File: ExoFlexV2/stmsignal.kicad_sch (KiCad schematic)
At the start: 4 parts, among them J4 CN8, J5 CN9, J6 CN7, J7 CN10

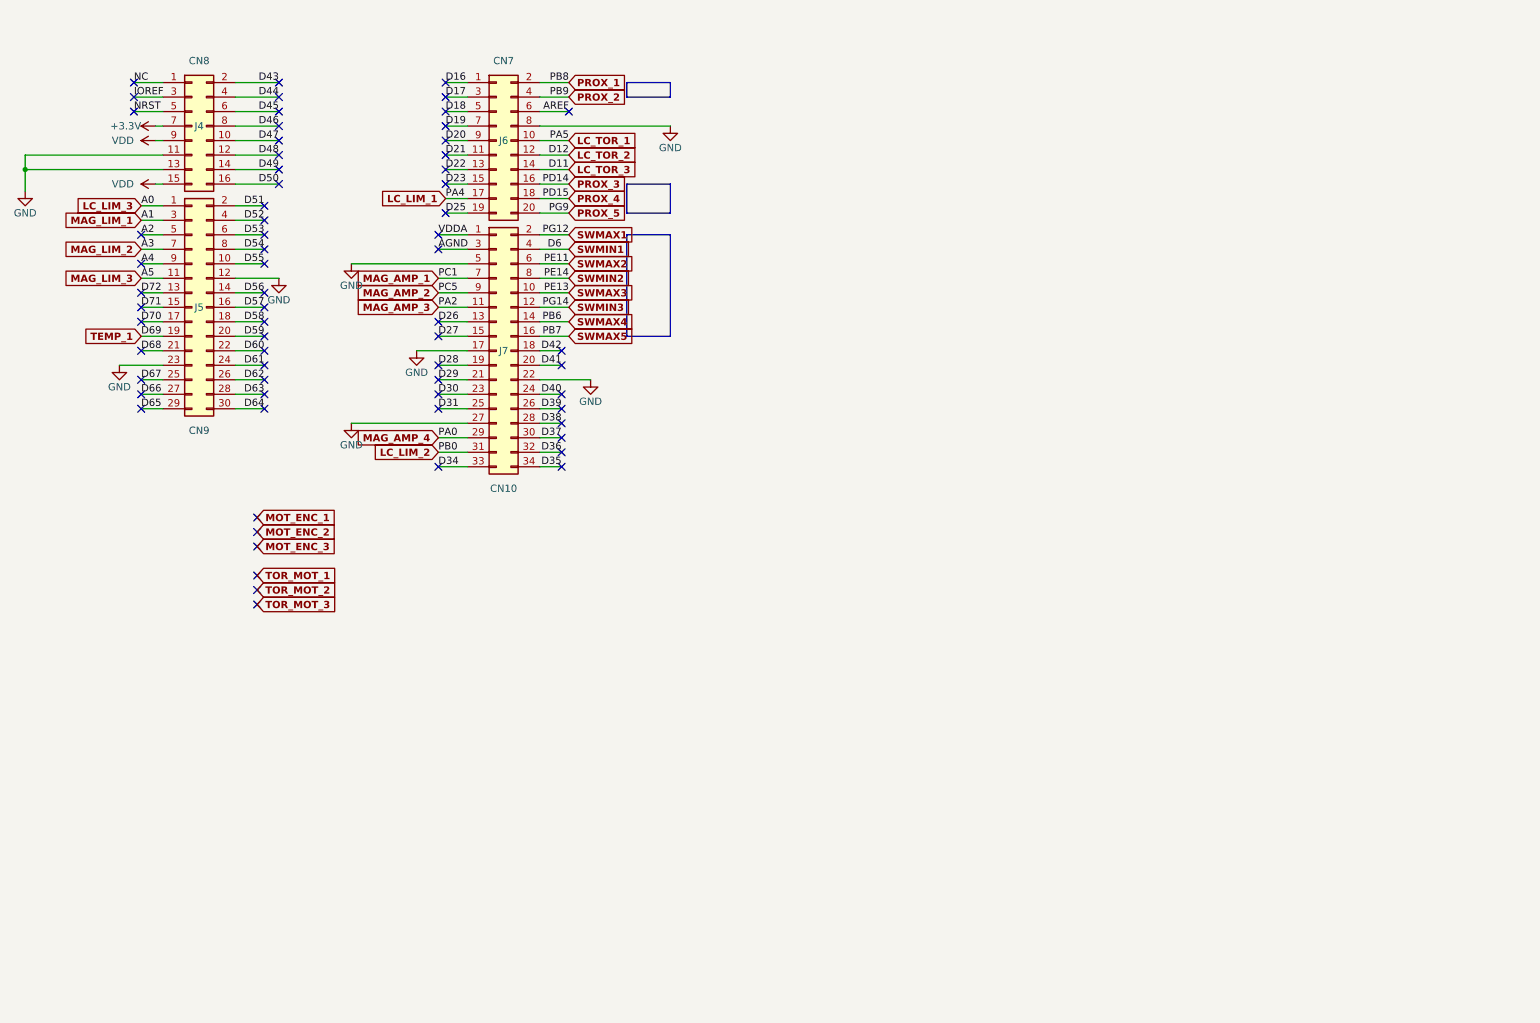
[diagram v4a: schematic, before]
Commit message: Mise à jour mi-stage
- Torque et Amplitude testé et vérifié
- Capteur de présence et de proximité testé
- Système de détection de coupure de fils
- Polyvalence pour plusieurs capteurs
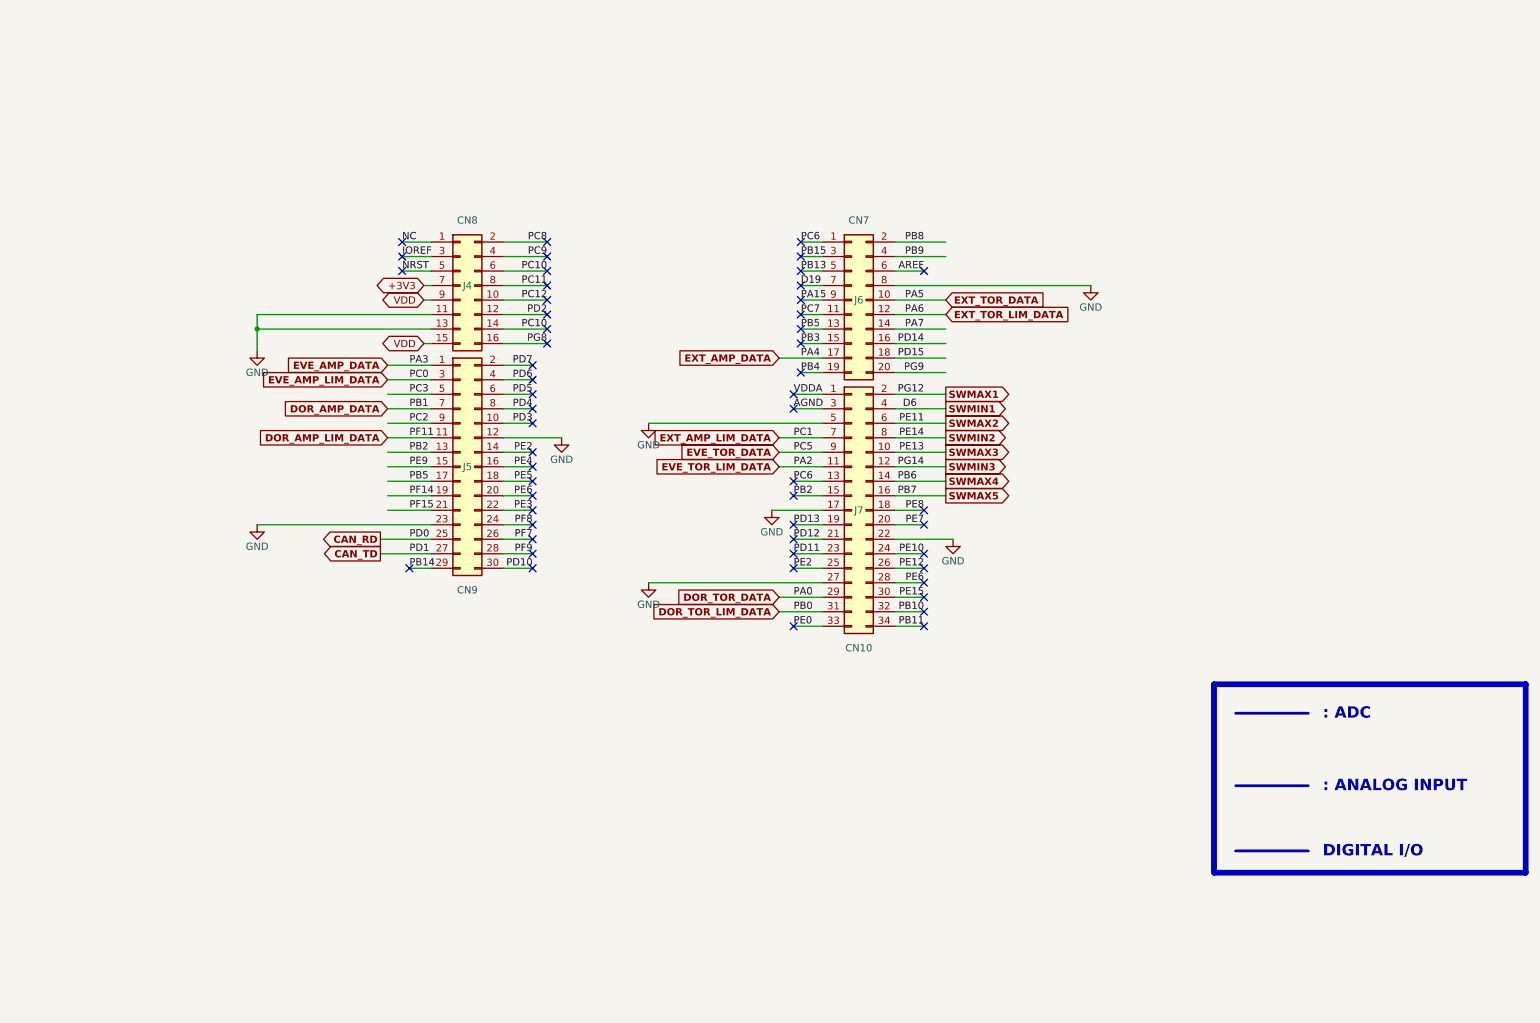
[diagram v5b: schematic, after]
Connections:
- net D26 is gone; now on net PC6: J7.13 (Pin_13)
- net D49 is gone; now on net PC10: J4.14 (Pin_14)
- net D56 is gone; now on net PE2: J5.14 (Pin_14)
- net D59 is gone; now on net PE6: J5.20 (Pin_20)
- net D70 is gone; now on net PB5: J5.17 (Pin_17)
- net D72 is gone; now on net PB2: J5.13 (Pin_13)
- net A2 renamed PC3
- net A4 renamed PC2
- net D16 renamed PC6
- net D17 renamed PB15
- net D18 renamed PB13
- net D20 renamed PA15
- net D21 renamed PC7
- net D22 renamed PB5
- net D23 renamed PB3
- net D25 renamed PB4
- net D27 renamed PB2
- net D28 renamed PD13
- net D29 renamed PD12
- net D30 renamed PD11
- net D31 renamed PE2
- net D34 renamed PE0
- net D35 renamed PB11
- net D36 renamed PB10
- net D37 renamed PE15
- net D38 renamed PE6
- net D39 renamed PE12
- net D40 renamed PE10
- net D41 renamed PE7
- net D42 renamed PE8
- net D43 renamed PC8
- net D44 renamed PC9
- net D45 renamed PC10
- net D46 renamed PC11
- net D47 renamed PC12
- net D48 renamed PD2
- net D50 renamed PG8
- net D51 renamed PD7
- net D52 renamed PD6
- net D53 renamed PD5
- net D54 renamed PD4
- net D55 renamed PD3
- net D57 renamed PE4
- net D58 renamed PE5
- net D60 renamed PE3
- net D61 renamed PF8
- net D62 renamed PF7
- net D63 renamed PF9
- net D64 renamed PD10
- net D65 renamed PB14
- net D66 renamed CAN_TD
- net D67 renamed CAN_RD
- net D68 renamed PF15
- net D71 renamed PE9
- net LC_LIM_1 renamed EXT_AMP_DATA
- net LC_LIM_2 renamed DOR_TOR_LIM_DATA
- net LC_LIM_3 renamed EVE_AMP_DATA
- net LC_TOR_1 renamed EXT_TOR_DATA
- net LC_TOR_2 renamed EXT_TOR_LIM_DATA
- net LC_TOR_3 renamed PA7
- net MAG_AMP_1 renamed EXT_AMP_LIM_DATA
- net MAG_AMP_2 renamed EVE_TOR_DATA
- net MAG_AMP_3 renamed EVE_TOR_LIM_DATA
- net MAG_AMP_4 renamed DOR_TOR_DATA
- net MAG_LIM_1 renamed EVE_AMP_LIM_DATA
- net MAG_LIM_2 renamed DOR_AMP_DATA
- net MAG_LIM_3 renamed DOR_AMP_LIM_DATA
- net PROX_1 renamed PB8
- net PROX_2 renamed PB9
- net PROX_3 renamed PD14
- net PROX_4 renamed PD15
- net PROX_5 renamed PG9
- net TEMP_1 renamed PF14
- no-connect marks 67 -> 53
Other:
- note added: ": ADC"
- note added: ": ANALOG INPUT"
- note added: "DIGITAL I/O"
- moved on the sheet: J4, J5, J6, J7

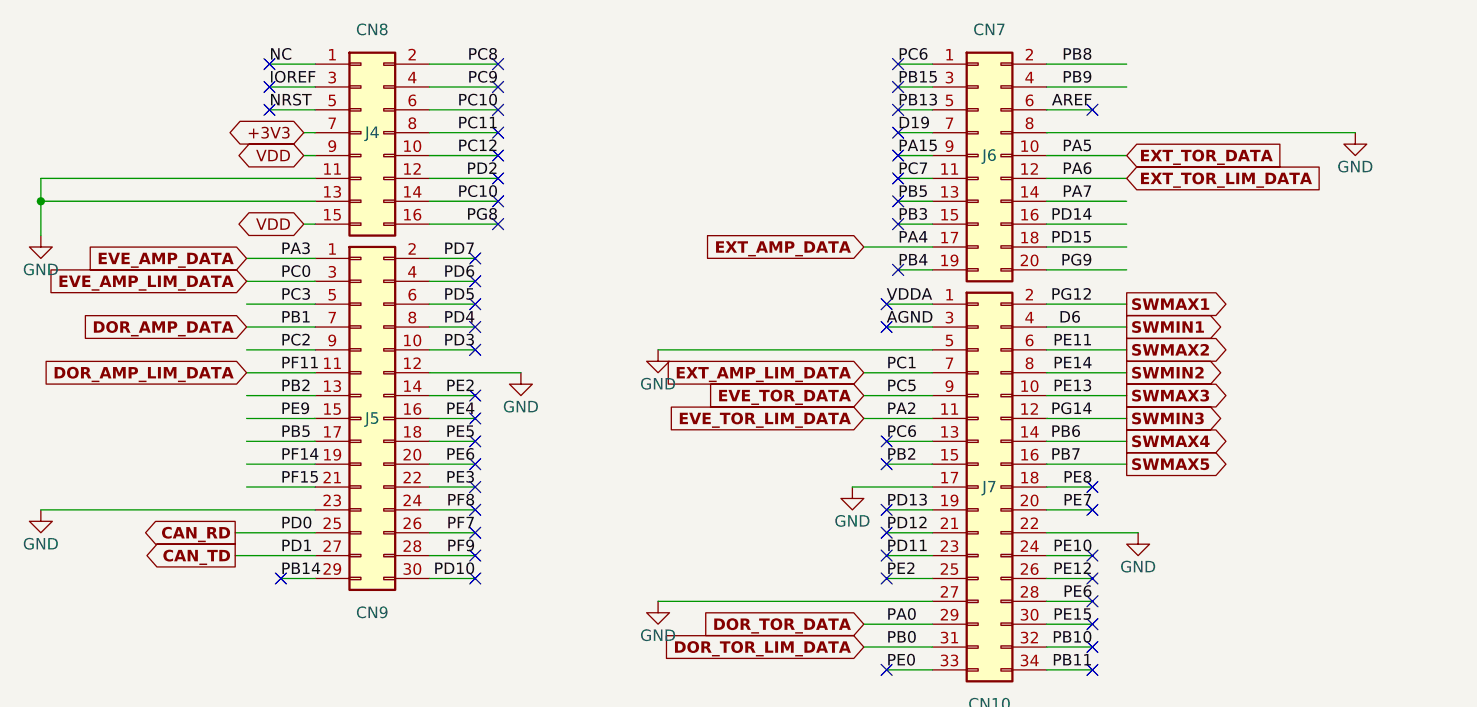
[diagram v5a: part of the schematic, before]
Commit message: Mise à jour signaux STM
- Condo de découplage
- Signaux supplémentaire pour le STM
- Page GND sera pour Multiplexeur
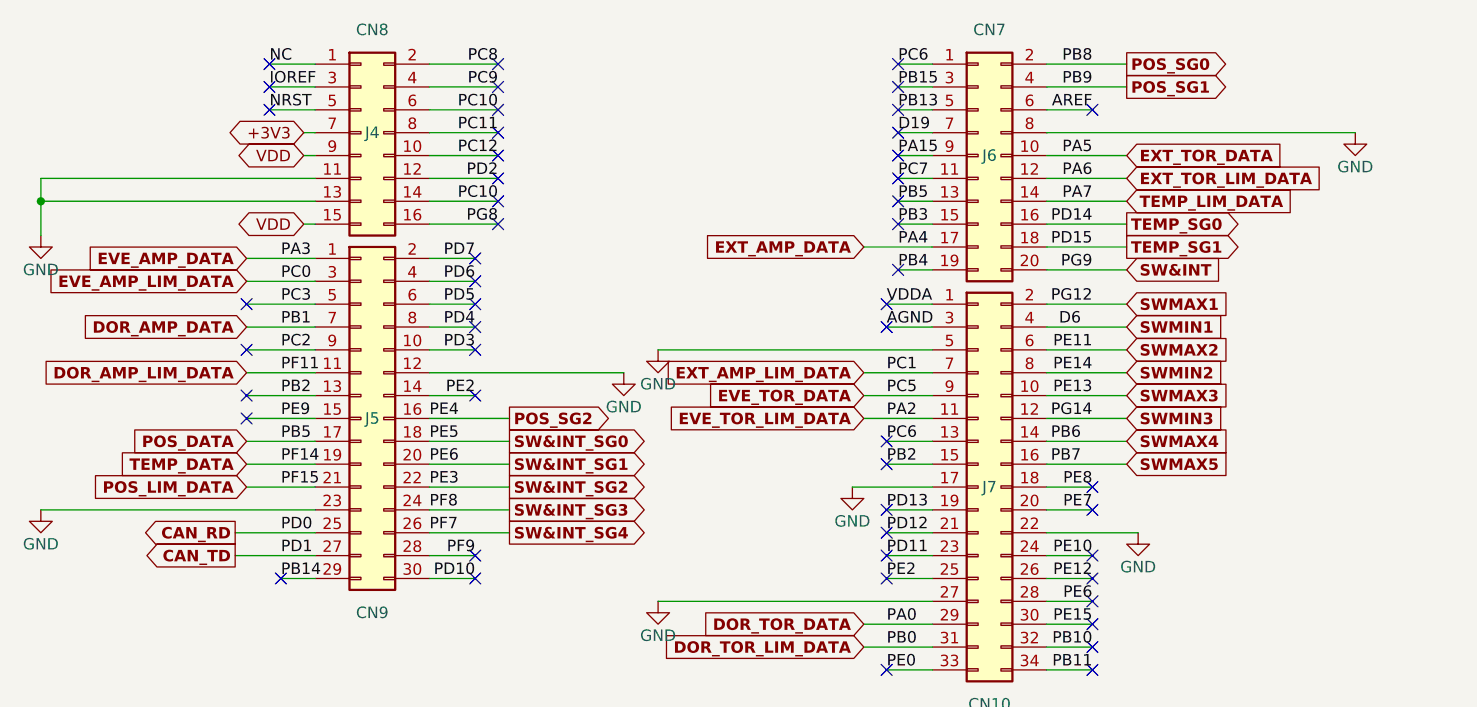
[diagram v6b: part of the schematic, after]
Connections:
- net PA7 renamed TEMP_LIM_DATA
- net PB5 renamed POS_DATA
- net PB8 renamed POS_SG0
- net PB9 renamed POS_SG1
- net PD14 renamed TEMP_SG0
- net PD15 renamed TEMP_SG1
- net PE3 renamed SW&INT_SG2
- net PE4 renamed POS_SG2
- net PE5 renamed SW&INT_SG0
- net PE6 renamed SW&INT_SG1
- net PF14 renamed TEMP_DATA
- net PF15 renamed POS_LIM_DATA
- net PF7 renamed SW&INT_SG4
- net PF8 renamed SW&INT_SG3
- net PG9 renamed SW&INT
- no-connect marks 53 -> 51
